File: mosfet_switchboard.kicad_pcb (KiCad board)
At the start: 2 copper layers, 115 x 55 mm, 103 parts, among them J1 Power Output, J2 Power Output, J3 Power Output, J4 Power Output, J5 Power Input, J6 Power Input, J7 USB_C_Receptacle_USB2.0, J8 Conn_01x04_Male, J9 Conn_ARM_JTAG_SWD_10, U1 BTS7004-1EPP, U2 BTS7004-1EPP, U3 BTS7004-1EPP, U4 BTS7004-1EPP, U5 AMS1117-3.3, U6 STM32F042C4Tx, U7 USBLC6-2SC6

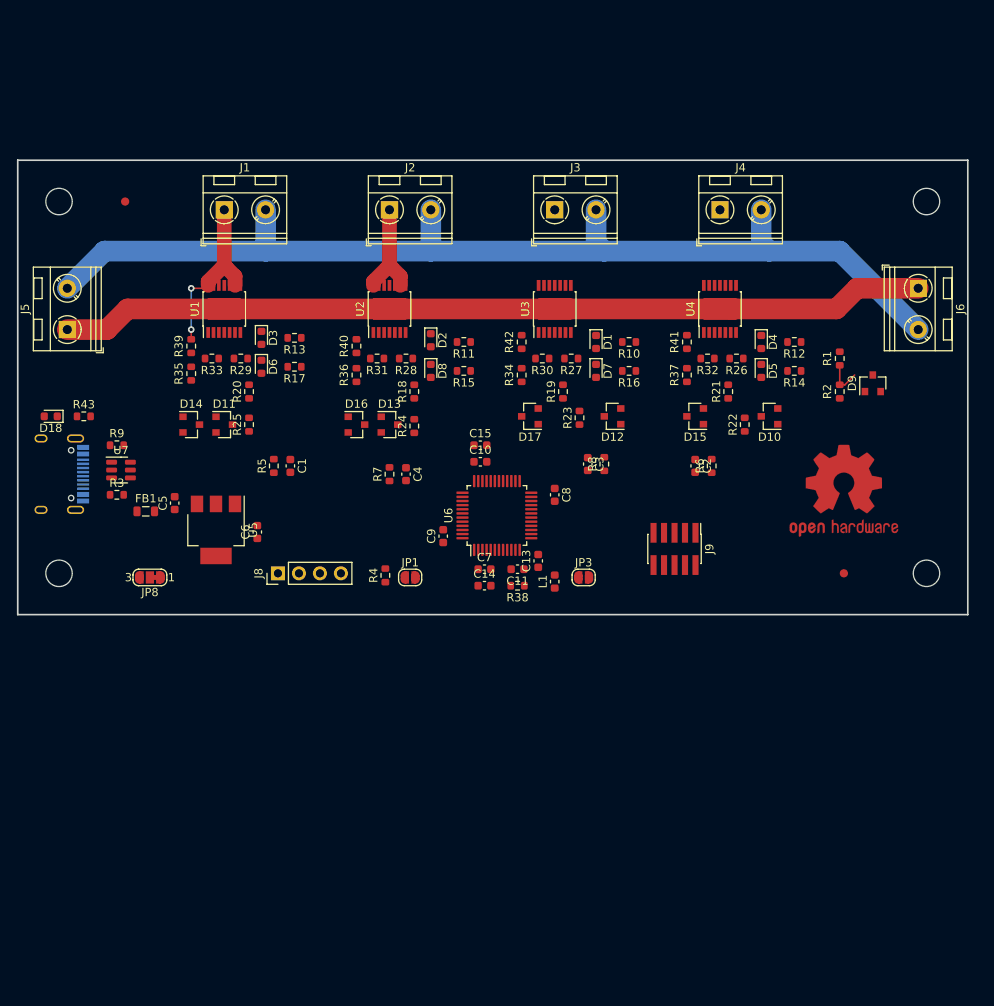
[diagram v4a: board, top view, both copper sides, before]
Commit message: layouting finished, some microcontroller connection rearrangements
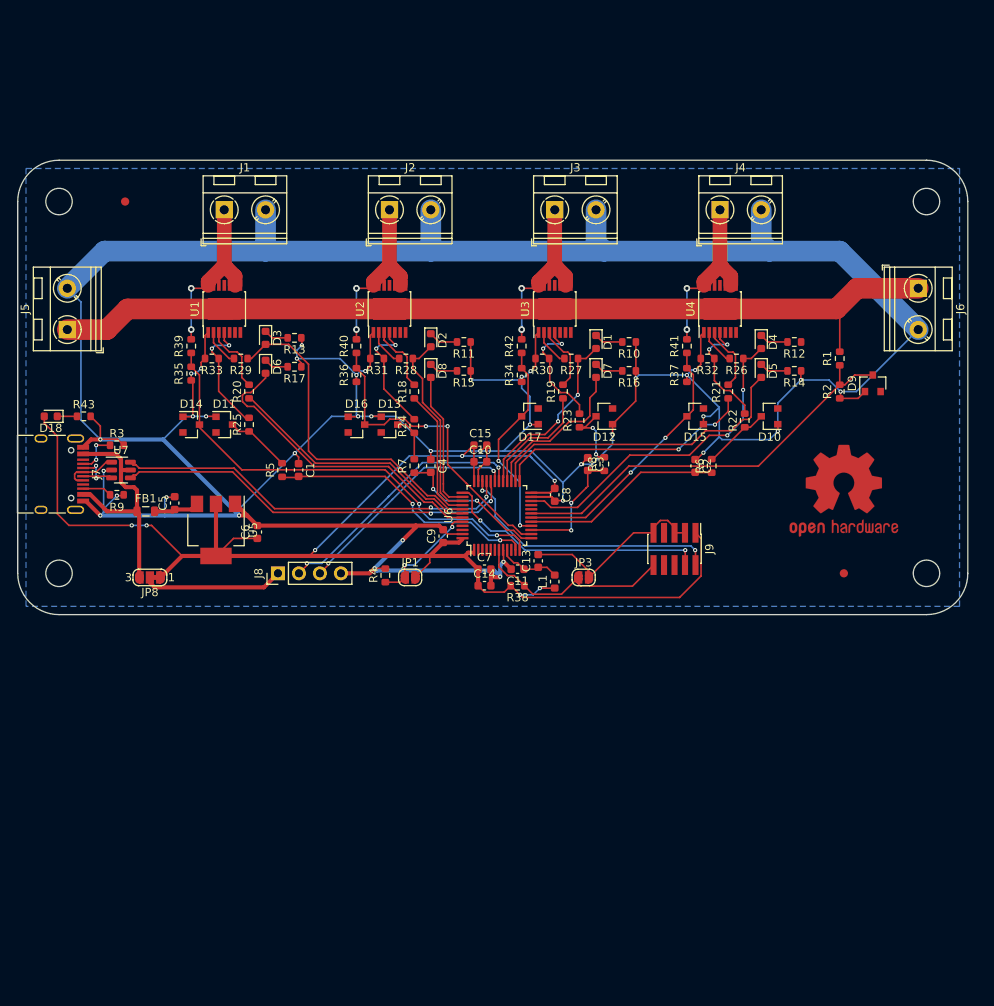
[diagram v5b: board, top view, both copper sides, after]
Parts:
- J7: moved to F.Cu
- moved R3 6.00 mm to (92.0, 74.5)
- moved R9 6.00 mm to (92.0, 80.5)
- moved C4 3.16 mm to (130.0, 77.0)
- moved R7 3.16 mm to (128.0, 77.0)
- moved C1 1.12 mm to (114.0, 77.5)
- moved R5 1.12 mm to (112.0, 77.5)
- moved D12 1.00 mm to (151.0, 71.0)
- moved D3 0.50 mm to (110.0, 61.5)
- moved D6 0.50 mm to (110.0, 65.0)
- moved R22 0.50 mm to (168.0, 71.5)
- moved R41 0.50 mm to (161.0, 62.5)
- moved R42 0.50 mm to (141.0, 62.5)
- moved R23 0.33 mm to (148.0, 71.5)
- turned J7 to -90 degrees
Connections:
- net /Control/USB_CONN_DM renamed /Control/USB_CONN_D-
- net /Control/USB_CONN_DP renamed /Control/USB_CONN_D+
- net /Control/USB_DM renamed /Control/USB_D-
- net /Control/USB_DP renamed /Control/USB_D+
- U6 pad 20: SW1_IN -> Net-(U6-Pad20)
- U6 pad 21: SW3_FAULT -> Net-(U6-Pad21)
- U6 pad 27: Net-(U6-Pad27) -> SW3_FAULT
- U6 pad 28: Net-(U6-Pad28) -> SW3_DEN
- U6 pad 29: Net-(U6-Pad29) -> SW3_IN
- U6 pad 38: Net-(U6-Pad38) -> SW2_FAULT
- U6 pad 39: SW1_DEN -> SW2_IN
- U6 pad 40: SW1_FAULT -> SW2_DEN
- U6 pad 41: SW2_IN -> SW1_IN
- U6 pad 42: SW2_DEN -> SW1_DEN
- U6 pad 43: SW2_FAULT -> SW1_FAULT
- U6 pad 45: SW3_IN -> Net-(U6-Pad45)
- U6 pad 46: SW3_DEN -> Net-(U6-Pad46)
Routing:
- net GND: track 129.6 -> 533.2 mm, vias 0 -> 38
- net +3V3: track 0.00 -> 179.8 mm, vias 0 -> 7
- net SW1_ADC_U: track 0.00 -> 55.3 mm, vias 0 -> 2
- net /Control/USB_D-: track 0.00 -> 49.2 mm, vias 0 -> 2
- net /Control/USB_D+: track 0.00 -> 48.2 mm, vias 0 -> 2
- net INPUT_ADC_U: track 4.64 -> 50.6 mm
- net SW1_IN: track 0.00 -> 41.2 mm
- net SW4_IN: track 0.00 -> 40.4 mm, vias 0 -> 2
- net SW4_FAULT: track 0.00 -> 38.3 mm
- net SW2_ADC_U: track 0.00 -> 38.0 mm, vias 0 -> 2
- net SW1_FAULT: track 0.00 -> 37.5 mm
- net /Control/SWDIO: track 0.00 -> 33.3 mm, vias 0 -> 2
- net SW1_ADC_I: track 0.00 -> 33.0 mm, vias 0 -> 2
- net /Control/SWCLK: track 0.00 -> 32.8 mm, vias 0 -> 2
- net SW4_ADC_U: track 0.00 -> 32.2 mm, vias 0 -> 2
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- added copper zone on B.Cu, net GND
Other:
- outline, holes or cut-outs redrawn

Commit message: use 1% resistor for voltage divider, add one more fiducial
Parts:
- added REF**: Fiducial_1mm_Mask2mm, Fiducial:Fiducial_1mm_Mask2mm, F.Cu at (180.0, 45.0)
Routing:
- net GND: track 533.2 -> 541.3 mm, vias 38 -> 39
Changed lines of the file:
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@@
     )
+  )
+  (module "Fiducial:Fiducial_1mm_Mask2mm" (layer "F.Cu")
+    (at 180 45)
+    (descr "Circular Fiducial, 1mm bare copper, 2mm soldermask opening (Level A)")
+    (tags "fiducial")
+    (attr smd)
+    (fp_text reference "REF**" (at 0 -2) (layer "F.SilkS") hide
+      (effects (font (size 1 1) (thickness 0.15)))
+    )
+    (fp_text value "Fiducial_1mm_Mask2mm" (at 0 2) (layer "F.Fab")
+      (effects (font (size 1 1) (thickness 0.15)))
+    )
+    (fp_text user "${REFERENCE}" (at 0 0) (layer "F.Fab")
+      (effects (font (size 0.4 0.4) (thickness 0.06)))
+    )
+    (fp_circle (center 0 0) (end 1.25 0) (layer "F.CrtYd") (width 0.05))
+    (fp_circle (center 0 0) (end 1 0) (layer "F.Fab") (width 0.1))
+    (pad "" smd circle (at 0 0) (size 1 1) (layers "F.Cu" "F.Mask")
+      (solder_mask_margin 0.5) (clearance 0.5))
   )
   (module "Resistor_SMD:R_0603_1608Metric" (layer "F.Cu")
@@
   (segment (start 138.8 88.6) (end 138.8 87.2125) (width 0.2) (layer "F.Cu") (net 2))
   (segment (start 146 81.2) (end 145.075 81.2) (width 0.2) (layer "F.Cu") (net 2))
+  (segment (start 174.825 65.5) (end 174.825 62) (width 0.2) (layer "F.Cu") (net 2))
   (segment (start 138.8 88.6) (end 138.825 88.6) (width 0.5) (layer "F.Cu") (net 2))
   (segment (start 103.95 71) (end 104 71.05) (width 0.2) (layer "F.Cu") (net 2))
@@
   (segment (start 124.475 89.4) (end 124.5 89.425) (width 0.2) (layer "F.Cu") (net 2))
   (segment (start 181.725 68.825) (end 179.5 68.825) (width 0.2) (layer "F.Cu") (net 2))
+  (segment (start 142.1 87.714) (end 142.989 87.714) (width 0.2) (layer "F.Cu") (net 2))
   (segment (start 107.7875 83.0125) (end 109 84.225) (width 0.5) (layer "F.Cu") (net 2))
   (segment (start 114.4 61.575) (end 114.325 61.5) (width 0.2) (layer "F.Cu") (net 2))
@@
   (segment (start 135.8 78.7875) (end 135.75 78.8375) (width 0.2) (layer "F.Cu") (net 2))
   (segment (start 142.675 64) (end 142.675 61.225) (width 0.2) (layer "F.Cu") (net 2))
+  (segment (start 142.989 87.714) (end 143 87.725) (width 0.2) (layer "F.Cu") (net 2))
   (segment (start 142 72) (end 142.95 72) (width 0.2) (layer "F.Cu") (net 2))
   (segment (start 174.8 65.525) (end 174.825 65.5) (width 0.2) (layer "F.Cu") (net 2))
@@
   (via (at 162 65.4) (size 0.508) (drill 0.254) (layers "F.Cu" "B.Cu") (net 2))
   (via (at 179.6 68) (size 0.508) (drill 0.254) (layers "F.Cu" "B.Cu") (net 2))
+  (via (at 142.1 87.714) (size 0.508) (drill 0.254) (layers "F.Cu" "B.Cu") (net 2))
   (via (at 142.075953 65.524047) (size 0.508) (drill 0.254) (layers "F.Cu" "B.Cu") (net 2))
   (via (at 90 83) (size 0.508) (drill 0.254) (layers "F.Cu" "B.Cu") (net 2))
@@
   (segment (start 170 50) (end 171 51) (width 2.5) (layer "B.Cu") (net 2))
   (segment (start 142.075953 65.524047) (end 142 65.6) (width 0.2) (layer "B.Cu") (net 2))
+  (segment (start 138.8 88.6) (end 141.214 88.6) (width 0.2) (layer "B.Cu") (net 2))
   (segment (start 118 71) (end 121.2 71) (width 0.2) (layer "B.Cu") (net 2))
   (segment (start 86 55.5) (end 90.5 51) (width 2.5) (layer "B.Cu") (net 2))
@@
   (segment (start 137.664001 89.664001) (end 138.4 90.4) (width 0.5) (layer "B.Cu") (net 2))
   (segment (start 122.075953 65.524047) (end 121.475953 65.524047) (width 0.2) (layer "B.Cu") (net 2))
+  (segment (start 141.214 88.6) (end 142.1 87.714) (width 0.2) (layer "B.Cu") (net 2))
   (segment (start 123.2 89.4) (end 126.6 86) (width 0.5) (layer "B.Cu") (net 2))
   (segment (start 179.6 68) (end 181.5 68) (width 0.2) (layer "B.Cu") (net 2))

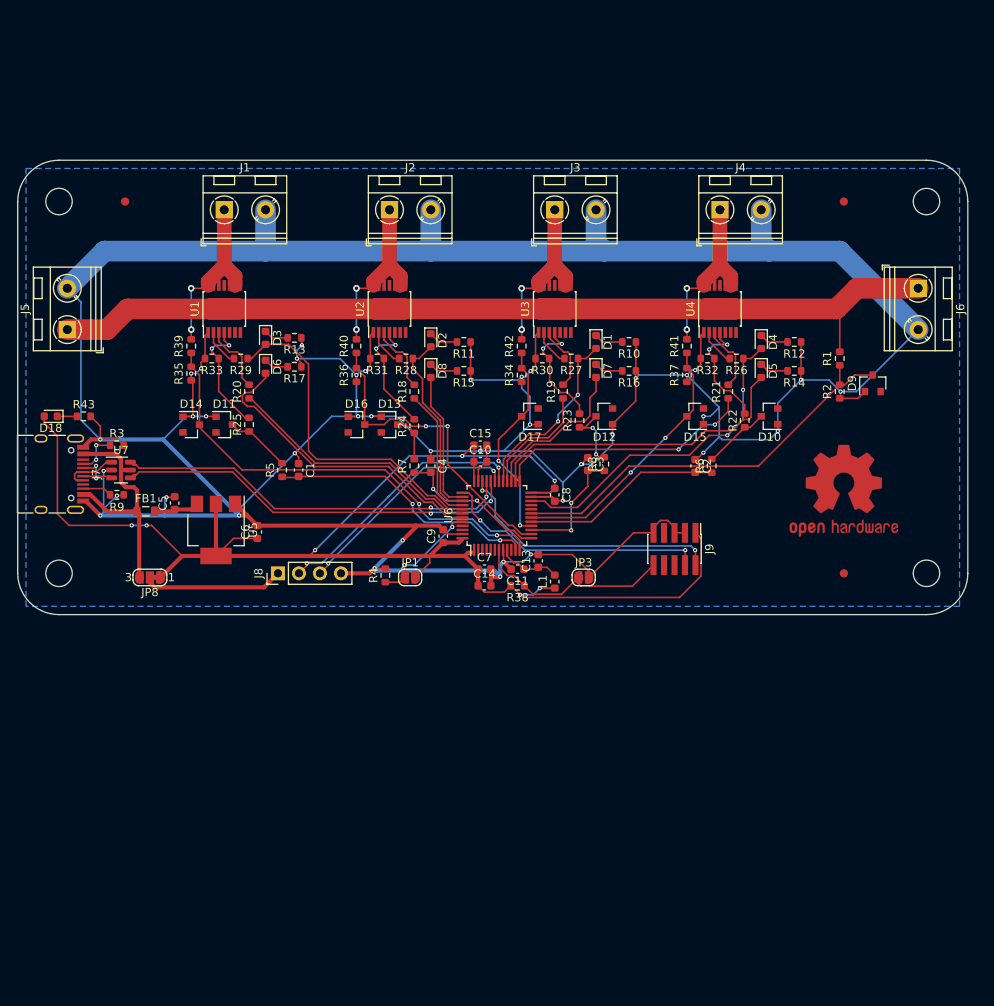
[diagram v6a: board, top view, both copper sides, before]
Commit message: add uC controlled status LED, improve filling zones, move LED closer to connectors
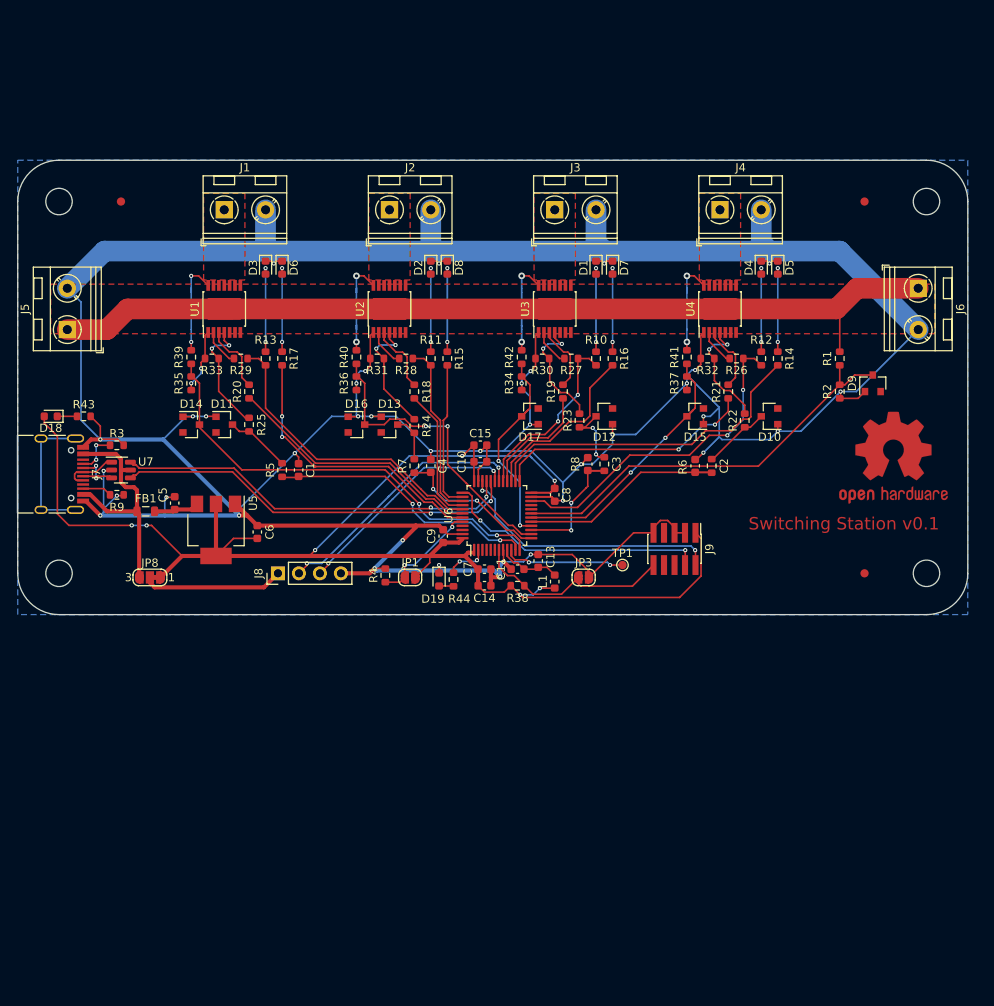
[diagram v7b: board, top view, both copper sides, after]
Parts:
- added D19: PINK, LED_SMD:LED_0603_1608Metric, F.Cu at (131.0, 90.8)
- added R44: 1kΩ, Resistor_SMD:R_0603_1608Metric, F.Cu at (132.8, 90.8)
- added TP1: TestPoint, TestPoint:TestPoint_Pad_D1.0mm, F.Cu at (153.2, 89.0)
- R1, R39, R40, R41, R42: value 12kΩ -> 12kΩ 1%
- R2, R34, R35, R36, R37: value 1.8kΩ -> 1.8kΩ 1%
- R30, R31, R32, R33: value 8.2kΩ -> 8.2kΩ 1%
- moved D5 12.7 mm to (172.0, 53.0)
- moved D7 12.7 mm to (152.0, 53.0)
- moved D8 12.7 mm to (132.0, 53.0)
- moved D6 12.2 mm to (112.0, 53.0)
- moved D1 9.00 mm to (150.0, 53.0)
- moved D4 9.00 mm to (170.0, 53.0)
- moved D2 8.79 mm to (130.0, 53.0)
- moved D3 8.50 mm to (110.0, 53.0)
- moved REF** 7.21 mm to (186.0, 76.0)
- moved R10 4.47 mm to (150.0, 64.0), turned to -90 degrees
- moved R11 4.47 mm to (130.0, 64.0), turned to -90 degrees
- moved R12 4.47 mm to (170.0, 64.0), turned to -90 degrees
- moved R13 4.30 mm to (110.0, 64.0), turned to -90 degrees
- moved R14 2.50 mm to (172.0, 64.0), turned to -90 degrees
- moved R15 2.50 mm to (132.0, 64.0), turned to -90 degrees
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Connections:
- D1 pad 1: Net-(D1-Pad1) -> GND
- D1 pad 2: SW3_IN -> Net-(D1-Pad2)
- D2 pad 1: Net-(D2-Pad1) -> GND
- D2 pad 2: SW2_IN -> Net-(D2-Pad2)
- D3 pad 1: Net-(D3-Pad1) -> GND
- D3 pad 2: SW1_IN -> Net-(D3-Pad2)
- D4 pad 1: Net-(D4-Pad1) -> GND
- D4 pad 2: SW4_IN -> Net-(D4-Pad2)
- D5 pad 1: Net-(D5-Pad1) -> GND
- D5 pad 2: SW4_FAULT -> Net-(D5-Pad2)
- D6 pad 1: Net-(D6-Pad1) -> GND
- D6 pad 2: SW1_FAULT -> Net-(D6-Pad2)
- D7 pad 1: Net-(D7-Pad1) -> GND
- D7 pad 2: SW3_FAULT -> Net-(D7-Pad2)
- D8 pad 1: Net-(D8-Pad1) -> GND
- D8 pad 2: SW2_FAULT -> Net-(D8-Pad2)
- R10 pad 1: GND -> Net-(D1-Pad2)
- R10 pad 2: Net-(D1-Pad1) -> SW3_IN
- R11 pad 1: GND -> Net-(D2-Pad2)
- R11 pad 2: Net-(D2-Pad1) -> SW2_IN
- R12 pad 1: GND -> Net-(D4-Pad2)
- R12 pad 2: Net-(D4-Pad1) -> SW4_IN
- R13 pad 1: GND -> Net-(D3-Pad2)
- R13 pad 2: Net-(D3-Pad1) -> SW1_IN
- R14 pad 1: GND -> Net-(D5-Pad2)
- R14 pad 2: Net-(D5-Pad1) -> SW4_FAULT
- R15 pad 1: GND -> Net-(D8-Pad2)
- R15 pad 2: Net-(D8-Pad1) -> SW2_FAULT
- R16 pad 1: GND -> Net-(D7-Pad2)
- R16 pad 2: Net-(D7-Pad1) -> SW3_FAULT
- R17 pad 1: GND -> Net-(D6-Pad2)
- R17 pad 2: Net-(D6-Pad1) -> SW1_FAULT
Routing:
- net GND: track 541.3 -> 512.9 mm
- net Net-(J7-PadS1): track 0.00 -> 17.0 mm
- net Net-(U6-Pad10): track 0.00 -> 14.7 mm, vias 0 -> 2
- net Net-(D2-Pad2): track 0.00 -> 11.0 mm, vias 0 -> 2
- net Net-(D8-Pad2): track 0.00 -> 10.8 mm, vias 0 -> 2
- net Net-(D7-Pad2): track 0.00 -> 10.8 mm, vias 0 -> 2
- net Net-(D6-Pad2): track 0.00 -> 10.8 mm, vias 0 -> 2
- net Net-(D5-Pad2): track 0.00 -> 10.8 mm, vias 0 -> 2
- net Net-(D4-Pad2): track 0.00 -> 10.8 mm, vias 0 -> 2
- net Net-(D3-Pad2): track 0.00 -> 10.8 mm, vias 0 -> 2
- net Net-(D1-Pad2): track 0.00 -> 10.8 mm, vias 0 -> 2
- net /Power/Power Switch 3/VDD_SWITCHED: track 21.8 -> 11.7 mm
- net /Power/Power Switch 4/VDD_SWITCHED: track 21.6 -> 12.0 mm
- net /Power/Power Switch 1/VDD_SWITCHED: track 21.3 -> 12.0 mm
- net /Power/Power Switch 2/VDD_SWITCHED: track 21.6 -> 12.5 mm
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- added copper zone on F.Cu, net /Power/Power Switch 1/VDD_SWITCHED
- added copper zone on F.Cu, net /Power/Power Switch 2/VDD_SWITCHED
- added copper zone on F.Cu, net /Power/Power Switch 3/VDD_SWITCHED
- added copper zone on F.Cu, net /Power/Power Switch 4/VDD_SWITCHED
- added copper zone on F.Cu, net VDD
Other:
- board text added: "Switching Station v0.1"
